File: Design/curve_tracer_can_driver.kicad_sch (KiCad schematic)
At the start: 26 parts, among them J501 CAN_In, J502 CAN_Out, U501 ADM3055E, U502 CDSOT23-T24CAN

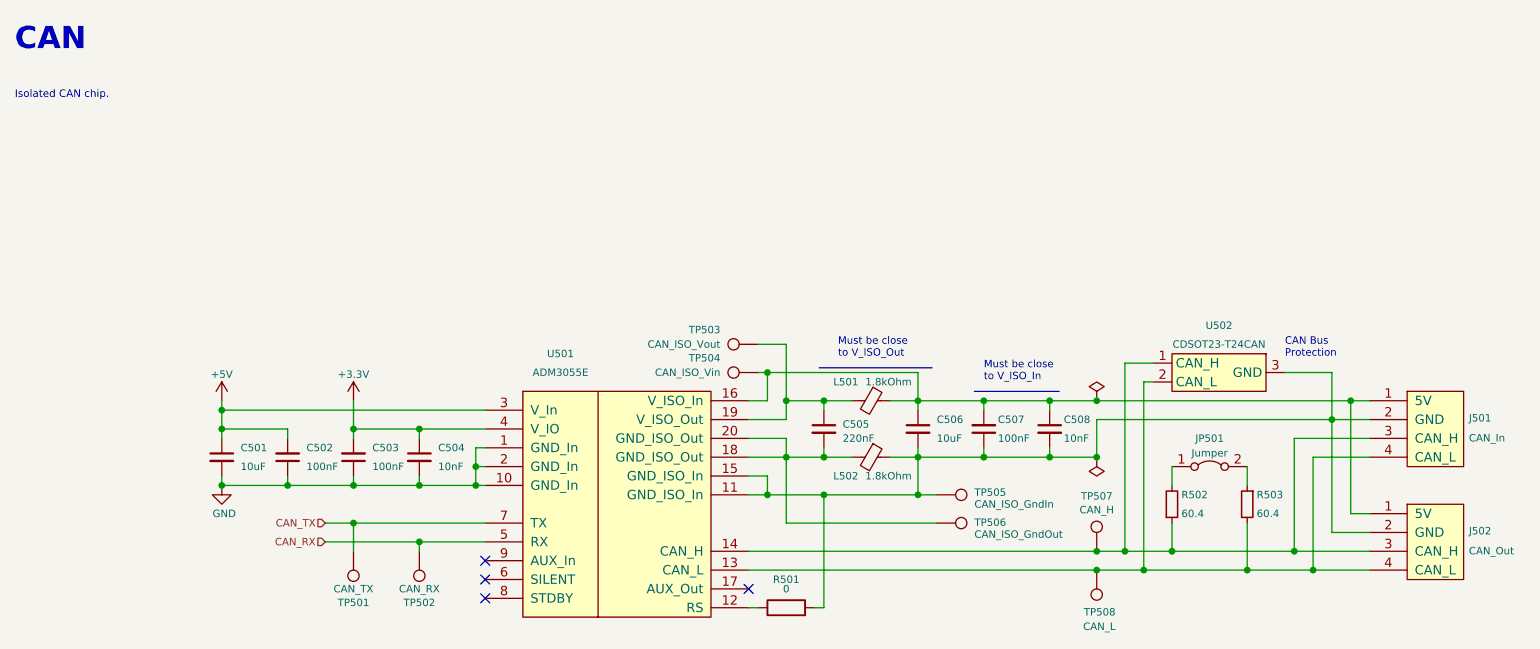
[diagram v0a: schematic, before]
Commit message: cleanup and fix errors for v1.3.0, proposed v1.4.0
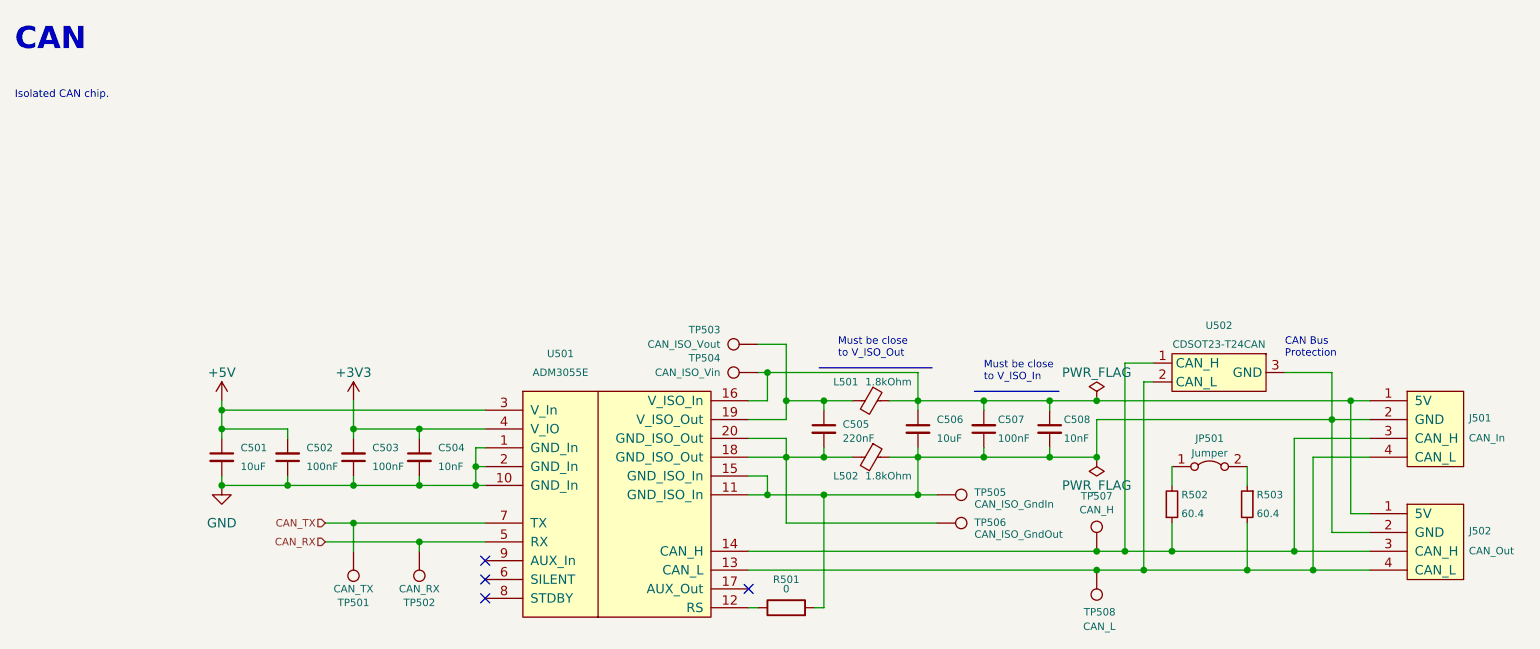
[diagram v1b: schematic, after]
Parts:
- C501, C506: Cost (none) -> 0.0131; JLCPCB BOM 1 -> (none); LCSC Part C15850 -> (none); LCSC Part # (none) -> C15850; Manufacturer Part Number CL21A106KAYNNNE -> (none); Mouser Part N/A -> (none); P/N (none) -> CL21A106KAYNNNE; Part Number N/A -> (none); Projected Cost 0.0141 -> (none); Purchase Page N/A -> (none)
- C502, C503, C507: Cost (none) -> 0.0078; JLCPCB BOM 1 -> (none); LCSC Part C28233 -> (none); LCSC Part # (none) -> C28233; Mouser Part N/A -> (none); P/N (none) -> CL21B104KCFNNNE; Part Number N/A -> (none); Projected Cost 0.0083 -> (none); Purchase Page N/A -> (none)
- C504, C508: Cost (none) -> 0.0085; JLCPCB BOM 1 -> (none); LCSC Part C1710 -> (none); LCSC Part # (none) -> C1710; Manufacturer Part Number CL21B103KBANNNC -> (none); Mouser Part N/A -> (none); P/N (none) -> CL21B103KBANNNC; Part Number N/A -> (none); Projected Cost 0.0057 -> (none); Purchase Page N/A -> (none)
- C505: Cost (none) -> 0.0116; JLCPCB BOM 1 -> (none); LCSC Part C5378 -> (none); LCSC Part # (none) -> C5378; Manufacturer Part Number CL21B224KBFNNNE -> (none); Mouser Part N/A -> (none); P/N (none) -> CL21B224KBFNNNE; Part Number N/A -> (none); Projected Cost 0.0118 -> (none); Purchase Page N/A -> (none)
- J501, J502: Cost (none) -> 1.19; JLCPCB BOM 0 -> (none); LCSC Part N/A -> (none); Manufacturer Part Number 43650-0427 -> (none); Mouser Part 538-43650-0427 -> (none); P/N (none) -> 43650-0415; Part Number 538-43650-0427 -> (none); Projected Cost 1.70 -> (none); Purchase Page https://www.mouser.com/ProductDetail/Molex/43650-0427?qs=yY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 -> (none)
- JP501: Cost (none) -> 0.10; Distributor (none) -> Mouser; Manufacturer (none) -> Amphenol FCI; P/N (none) -> 10129378-902004BLF; Part Number N/A -> (none)
- L501, L502: Cost (none) -> 0.17; JLCPCB BOM 0 -> (none); LCSC Part N/A -> (none); Manufacturer Part Number BLM21BD182SN1D -> (none); Mouser Part 81-BLM21BD182SN1D -> (none); P/N (none) -> BLM21BD182SN1D; Part Number 81-BLM21BD182SN1D -> (none); Projected Cost 0.23 -> (none); Purchase Page https://www.mouser.com/ProductDetail/Murata-Electronics/BLM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 -> (none)
- R501: Cost (none) -> 0.0022; JLCPCB BOM 1 -> (none); LCSC Part C17477 -> (none); LCSC Part # (none) -> C17477; Manufacturer Uniroyal Elec -> UNI-ROYAL(Uniroyal Elec); Manufacturer Part Number 0805W8F0000T5E -> (none); Mouser Part N/A -> (none); P/N (none) -> 0805W8F0000T5E; Part Number N/A -> (none); Projected Cost 0.0023 -> (none); Purchase Page N/A -> (none)
- R502, R503: Cost (none) -> 0.10; JLCPCB BOM 0 -> (none); LCSC Part N/A -> (none); Manufacturer Vishay/Dale -> Yageo; Manufacturer Part Number CRCW080560R4FKEAHP -> (none); Mouser Part 71-CRCW080560R4FKEAH -> (none); P/N (none) -> AC0805FR-7W60R4L; Part Number 71-CRCW080560R4FKEAH -> (none); Projected Cost 0.25 -> (none); Purchase Page https://www.mouser.com/ProductDetail/Vishay-Dale/CRCW080560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 -> (none)
- TP501, TP502, TP503, TP504, TP505, TP506, TP507, TP508: Part Number N/A -> (none)
- U501: Cost (none) -> 15.22; JLCPCB BOM 0 -> (none); LCSC Part N/A -> (none); Manufacturer Part Number ADM3055EBRIZ -> (none); Mouser Part 584-ADM3055EBRIZ -> (none); P/N (none) -> ADM3055EBRIZ; Part Number 584-ADM3055EBRIZ -> (none); Projected Cost 14.91 -> (none); Purchase Page https://www.mouser.com/ProductDetail/Analog-Devices/ADM3055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 -> (none)
- U502: Cost (none) -> 0.37; JLCPCB BOM 0 -> (none); LCSC Part N/A -> (none); Manufacturer Part Number CDSOT23-T24CAN-Q -> (none); Mouser Part 652-CDSOT23-T24CAN-Q -> (none); P/N (none) -> CDSOT23-T24CAN-Q; Part Number 652-CDSOT23-T24CAN-Q -> (none); Projected Cost 0.50 -> (none); Purchase Page https://www.mouser.com/ProductDetail/Bourns/CDSOT23-T24CAN-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 -> (none)
